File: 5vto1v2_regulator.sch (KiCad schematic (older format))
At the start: 10 parts

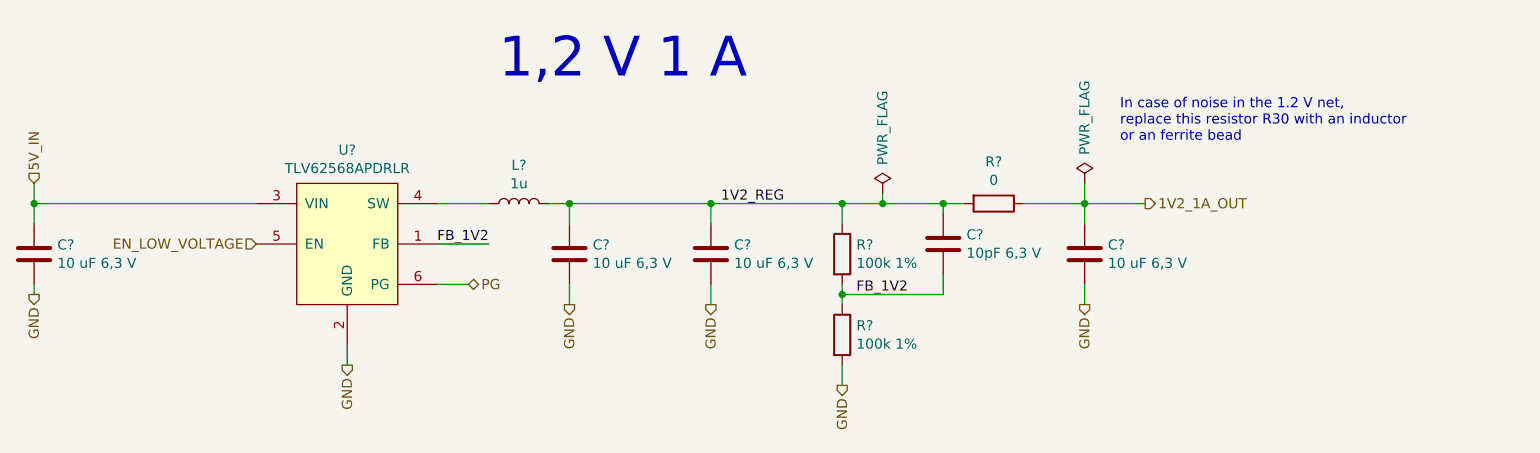
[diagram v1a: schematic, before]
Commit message: Schematic modified (Hierarchy) Bug where SPI was active when creset or ss was low fixed PCB layout started (almost all parts are at position) No parts on the bottom so far Arduino and PMOD header spacings corrected according to its standards
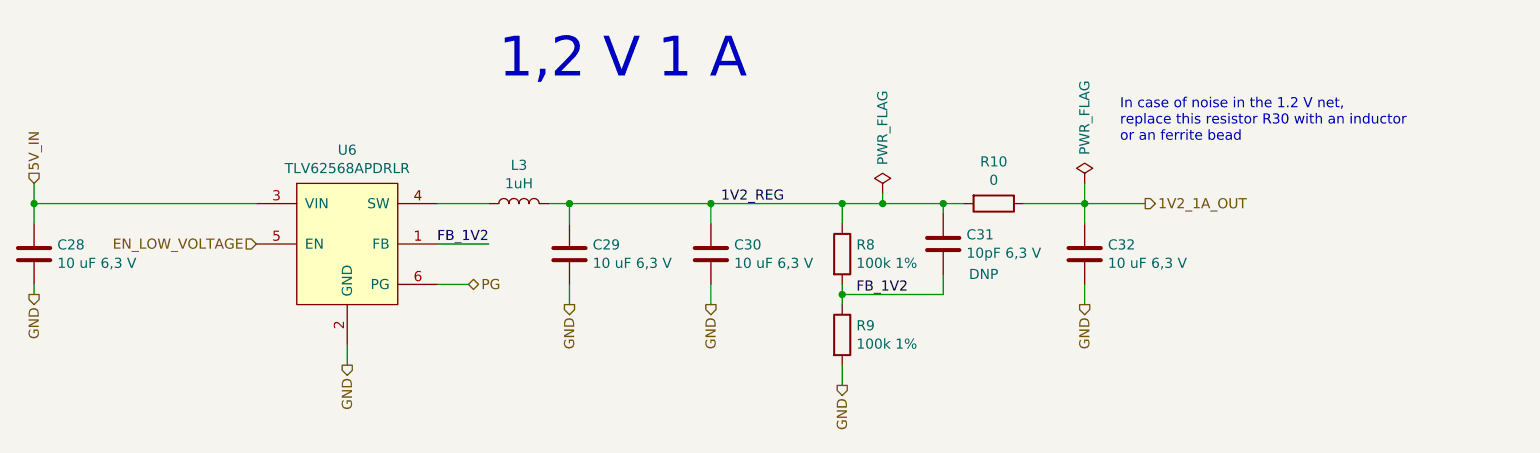
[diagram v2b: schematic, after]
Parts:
- C31: renamed from C?; DNP (none) -> DNP
- L3: renamed from L?; value 1u -> 1uH
- gave numbers to parts that had none: 8
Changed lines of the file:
@@
 $Descr A4 11693 8268
 encoding utf-8
-Sheet 5 7
+Sheet 5 14
 Title ""
 Date ""
@@
 P 2650 2050
 AR Path="/5ECD2614/5F68EB6F" Ref="U?"  Part="1"
-AR Path="/5ECD2614/5F6750DD/5F68EB6F" Ref="U?"  Part="1"
-F 0 "U?" H 2650 2515 50  0000 C CNN
+AR Path="/5ECD2614/5F6750DD/5F68EB6F" Ref="U6"  Part="1"
+F 0 "U6" H 2650 2515 50  0000 C CNN
 F 1 "TLV62568APDRLR" H 2650 2424 50  0000 C CNN
 F 2 "footprints:Texas_DRL_SOT-563_1.6x1.6mm_0.5mm-pitch_footprint" H 2650 1750 50  0001 C CNN
@@
 P 1100 2100
 AR Path="/5ECD2614/5F68EB7A" Ref="C?"  Part="1"
-AR Path="/5ECD2614/5F6750DD/5F68EB7A" Ref="C?"  Part="1"
-F 0 "C?" H 1215 2146 50  0000 L CNN
+AR Path="/5ECD2614/5F6750DD/5F68EB7A" Ref="C28"  Part="1"
+F 0 "C28" H 1215 2146 50  0000 L CNN
 F 1 "10 uF 6,3 V" H 1215 2055 50  0000 L CNN
 F 2 "Capacitor_SMD:C_0603_1608Metric" H 1138 1950 50  0001 C CNN
@@
 P 3750 2100
 AR Path="/5ECD2614/5F68EB85" Ref="C?"  Part="1"
-AR Path="/5ECD2614/5F6750DD/5F68EB85" Ref="C?"  Part="1"
-F 0 "C?" H 3865 2146 50  0000 L CNN
+AR Path="/5ECD2614/5F6750DD/5F68EB85" Ref="C29"  Part="1"
+F 0 "C29" H 3865 2146 50  0000 L CNN
 F 1 "10 uF 6,3 V" H 3865 2055 50  0000 L CNN
 F 2 "Capacitor_SMD:C_0603_1608Metric" H 3788 1950 50  0001 C CNN
@@
 P 5100 2100
 AR Path="/5ECD2614/5F68EB90" Ref="R?"  Part="1"
-AR Path="/5ECD2614/5F6750DD/5F68EB90" Ref="R?"  Part="1"
-F 0 "R?" H 5170 2146 50  0000 L CNN
+AR Path="/5ECD2614/5F6750DD/5F68EB90" Ref="R8"  Part="1"
+F 0 "R8" H 5170 2146 50  0000 L CNN
 F 1 "100k 1%" H 5170 2055 50  0000 L CNN
 F 2 "Resistor_SMD:R_0603_1608Metric" V 5030 2100 50  0001 C CNN
@@
 P 5100 2500
 AR Path="/5ECD2614/5F68EB9B" Ref="R?"  Part="1"
-AR Path="/5ECD2614/5F6750DD/5F68EB9B" Ref="R?"  Part="1"
-F 0 "R?" H 5170 2546 50  0000 L CNN
+AR Path="/5ECD2614/5F6750DD/5F68EB9B" Ref="R9"  Part="1"
+F 0 "R9" H 5170 2546 50  0000 L CNN
 F 1 "100k 1%" H 5170 2455 50  0000 L CNN
 F 2 "Resistor_SMD:R_0603_1608Metric" V 5030 2500 50  0001 C CNN
@@
 P 3500 1850
 AR Path="/5ECD2614/5F68EBC9" Ref="L?"  Part="1"
-AR Path="/5ECD2614/5F6750DD/5F68EBC9" Ref="L?"  Part="1"
-F 0 "L?" V 3690 1850 50  0000 C CNN
-F 1 "1u" V 3599 1850 50  0000 C CNN
+AR Path="/5ECD2614/5F6750DD/5F68EBC9" Ref="L3"  Part="1"
+F 0 "L3" V 3690 1850 50  0000 C CNN
+F 1 "1uH" V 3599 1850 50  0000 C CNN
 F 2 "footprints:L_1008_2520Metric_2.5x2mm_footprint" H 3500 1850 50  0001 C CNN
 F 3 "https://www.yuden.co.jp/productdata/catalog/wound10_e.pdf" H 3500 1850 50  0001 C CNN
@@
 P 5600 2050
 AR Path="/5ECD2614/5F68EBDE" Ref="C?"  Part="1"
-AR Path="/5ECD2614/5F6750DD/5F68EBDE" Ref="C?"  Part="1"
-F 0 "C?" H 5715 2096 50  0000 L CNN
+AR Path="/5ECD2614/5F6750DD/5F68EBDE" Ref="C31"  Part="1"
+F 0 "C31" H 5715 2096 50  0000 L CNN
 F 1 "10pF 6,3 V" H 5715 2005 50  0000 L CNN
 F 2 "Capacitor_SMD:C_0603_1608Metric" H 5638 1900 50  0001 C CNN
@@
 F 7 "CL10C100JB8NNNC" H -175 -5300 50  0001 C CNN "Mfg Part Num"
 F 8 "Any" H -175 -5300 50  0001 C CNN "Spec"
+F 9 "DNP" H 5800 1900 50  0000 C CNN "DNP"
 	1    5600 2050
 	1    0    0    -1
@@
 P 5300 1800
 AR Path="/5ECD2614/5F68EBE8" Ref="#FLG?"  Part="1"
-AR Path="/5ECD2614/5F6750DD/5F68EBE8" Ref="#FLG?"  Part="1"
-F 0 "#FLG?" H 5300 1875 50  0001 C CNN
+AR Path="/5ECD2614/5F6750DD/5F68EBE8" Ref="#FLG05"  Part="1"
+F 0 "#FLG05" H 5300 1875 50  0001 C CNN
 F 1 "PWR_FLAG" V 5300 2125 50  0000 C CNN
 F 2 "" H 5300 1800 50  0001 C CNN
@@
 P 5850 1850
 AR Path="/5ECD2614/5F68EC06" Ref="R?"  Part="1"
-AR Path="/5ECD2614/5F6750DD/5F68EC06" Ref="R?"  Part="1"
-F 0 "R?" V 5643 1850 50  0000 C CNN
+AR Path="/5ECD2614/5F6750DD/5F68EC06" Ref="R10"  Part="1"
+F 0 "R10" V 5643 1850 50  0000 C CNN
 F 1 "0" V 5734 1850 50  0000 C CNN
 F 2 "Resistor_SMD:R_0805_2012Metric" V 5780 1850 50  0001 C CNN
@@
 P 6300 1750
 AR Path="/5ECD2614/5F68EC0E" Ref="#FLG?"  Part="1"
-AR Path="/5ECD2614/5F6750DD/5F68EC0E" Ref="#FLG?"  Part="1"
-F 0 "#FLG?" H 6300 1825 50  0001 C CNN
+AR Path="/5ECD2614/5F6750DD/5F68EC0E" Ref="#FLG06"  Part="1"
+F 0 "#FLG06" H 6300 1825 50  0001 C CNN
 F 1 "PWR_FLAG" V 6300 2075 50  0000 C CNN
 F 2 "" H 6300 1750 50  0001 C CNN
@@
 P 4450 2100
 AR Path="/5ECD2614/5F68EC24" Ref="C?"  Part="1"
-AR Path="/5ECD2614/5F6750DD/5F68EC24" Ref="C?"  Part="1"
-F 0 "C?" H 4565 2146 50  0000 L CNN
+AR Path="/5ECD2614/5F6750DD/5F68EC24" Ref="C30"  Part="1"
+F 0 "C30" H 4565 2146 50  0000 L CNN
 F 1 "10 uF 6,3 V" H 4565 2055 50  0000 L CNN
 F 2 "Capacitor_SMD:C_0603_1608Metric" H 4488 1950 50  0001 C CNN
@@
 P 6300 2100
 AR Path="/5ECD2614/5F68EC2F" Ref="C?"  Part="1"
-AR Path="/5ECD2614/5F6750DD/5F68EC2F" Ref="C?"  Part="1"
-F 0 "C?" H 6415 2146 50  0000 L CNN
+AR Path="/5ECD2614/5F6750DD/5F68EC2F" Ref="C32"  Part="1"
+F 0 "C32" H 6415 2146 50  0000 L CNN
 F 1 "10 uF 6,3 V" H 6415 2055 50  0000 L CNN
 F 2 "Capacitor_SMD:C_0603_1608Metric" H 6338 1950 50  0001 C CNN
